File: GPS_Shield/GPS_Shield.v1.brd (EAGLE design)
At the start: 31.8 x 37.8 mm, 11 parts, among them T1 2N2222, U1 USD-SOCKETMOLEX-CORRECT

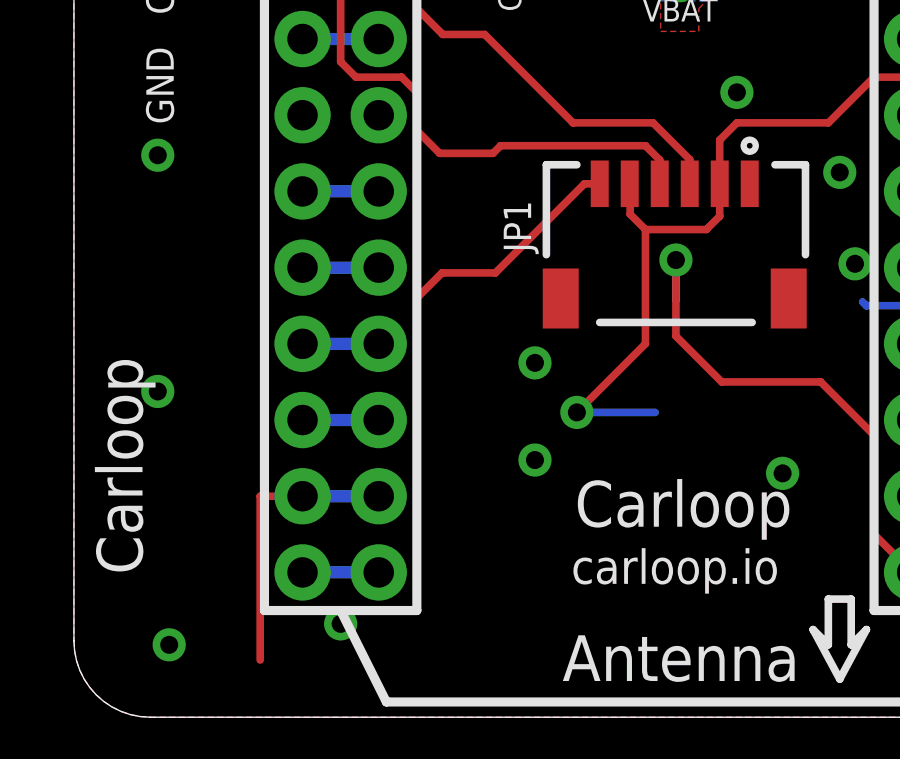
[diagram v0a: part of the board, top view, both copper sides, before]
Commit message: Add GPS_EN
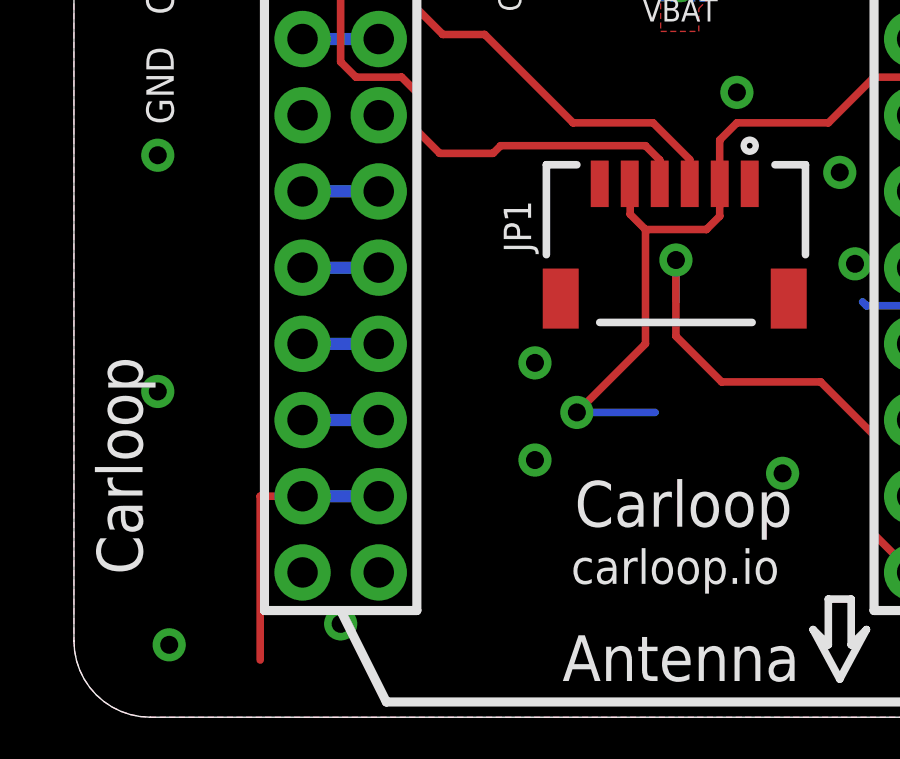
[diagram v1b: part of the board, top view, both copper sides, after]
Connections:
- removed net N$14: CORE.18, CORE.@18
- removed net N$15: CORE.17, CORE.@17
- new net GPS_EN: CORE.12, CORE.@12, GPS.19, JP1.6
- net PPS_EN: now also CORE.17, CORE.18, CORE.@17, CORE.@18; no longer CORE.12, CORE.@12, JP1.6
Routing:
- net PPS_EN: track 18.1 -> 5.08 mm
- net N$15: track 2.54 -> 0.00 mm
- net N$14: track 2.54 -> 0.00 mm
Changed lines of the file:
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@@
 <wire x1="31.242" y1="19.812" x2="28.702" y2="19.812" width="0.4064" layer="16"/>
-</signal>
-<signal name="N$14">
-<contactref element="CORE" pad="@18"/>
-<contactref element="CORE" pad="18"/>
-<wire x1="31.242" y1="17.272" x2="28.702" y2="17.272" width="0.4064" layer="16"/>
-</signal>
-<signal name="N$15">
-<contactref element="CORE" pad="@17"/>
-<contactref element="CORE" pad="17"/>
-<wire x1="31.242" y1="14.732" x2="28.702" y2="14.732" width="0.4064" layer="16"/>
 </signal>
 <signal name="N$26">
@@
 <signal name="PPS_EN">
 <contactref element="D1" pad="A"/>
-<contactref element="CORE" pad="12"/>
-<contactref element="CORE" pad="@12"/>
-<wire x1="10.922" y1="4.572" x2="8.382" y2="4.572" width="0.4064" layer="16"/>
-<contactref element="JP1" pad="6"/>
-<wire x1="18.288" y1="17.526" x2="17.78" y2="17.526" width="0.254" layer="1"/>
-<wire x1="14.8082" y1="14.5542" x2="13.0302" y2="14.5542" width="0.254" layer="1"/>
-<wire x1="13.0302" y1="14.5542" x2="12.192" y2="13.716" width="0.254" layer="1"/>
-<wire x1="12.192" y1="13.716" x2="12.192" y2="5.842" width="0.254" layer="1"/>
-<wire x1="14.8082" y1="14.5542" x2="17.78" y2="17.526" width="0.254" layer="1"/>
-<wire x1="8.382" y1="4.572" x2="-58.293" y2="-64.758" width="0" layer="19" extent="1-1"/>
-<wire x1="12.192" y1="5.842" x2="10.922" y2="4.572" width="0" layer="19" extent="1-1"/>
+<contactref element="CORE" pad="@18"/>
+<contactref element="CORE" pad="18"/>
+<wire x1="31.242" y1="17.272" x2="28.702" y2="17.272" width="0.4064" layer="16"/>
+<contactref element="CORE" pad="@17"/>
+<contactref element="CORE" pad="17"/>
+<wire x1="31.242" y1="14.732" x2="28.702" y2="14.732" width="0.4064" layer="16"/>
+<wire x1="28.702" y1="14.732" x2="-58.293" y2="-64.758" width="0" layer="19" extent="1-1"/>
+<wire x1="31.242" y1="17.272" x2="31.242" y2="14.732" width="0" layer="19" extent="1-1"/>
 </signal>
 <signal name="RST">
@@
 <wire x1="8.382" y1="19.812" x2="10.922" y2="19.812" width="0" layer="19" extent="1-1"/>
 </signal>
+<signal name="GPS_EN">
+<contactref element="CORE" pad="12"/>
+<contactref element="CORE" pad="@12"/>
+<contactref element="JP1" pad="6"/>
+<contactref element="GPS" pad="19"/>
+<wire x1="8.382" y1="4.572" x2="-9.017" y2="-58.039" width="0" layer="19" extent="1-1"/>
+<wire x1="10.922" y1="4.572" x2="8.382" y2="4.572" width="0" layer="19" extent="1-1"/>
+<wire x1="18.288" y1="17.526" x2="10.922" y2="4.572" width="0" layer="19" extent="1-1"/>
+</signal>
 </signals>

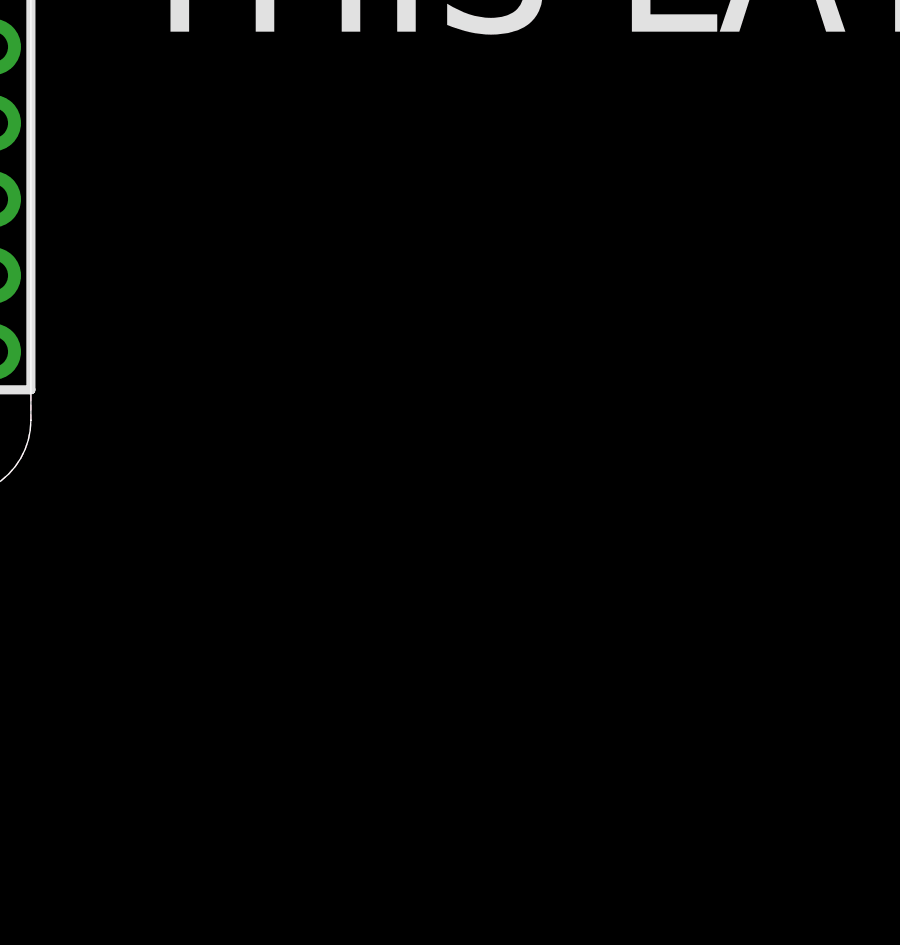
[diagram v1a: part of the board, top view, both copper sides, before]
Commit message: Tweaks for silkscreen
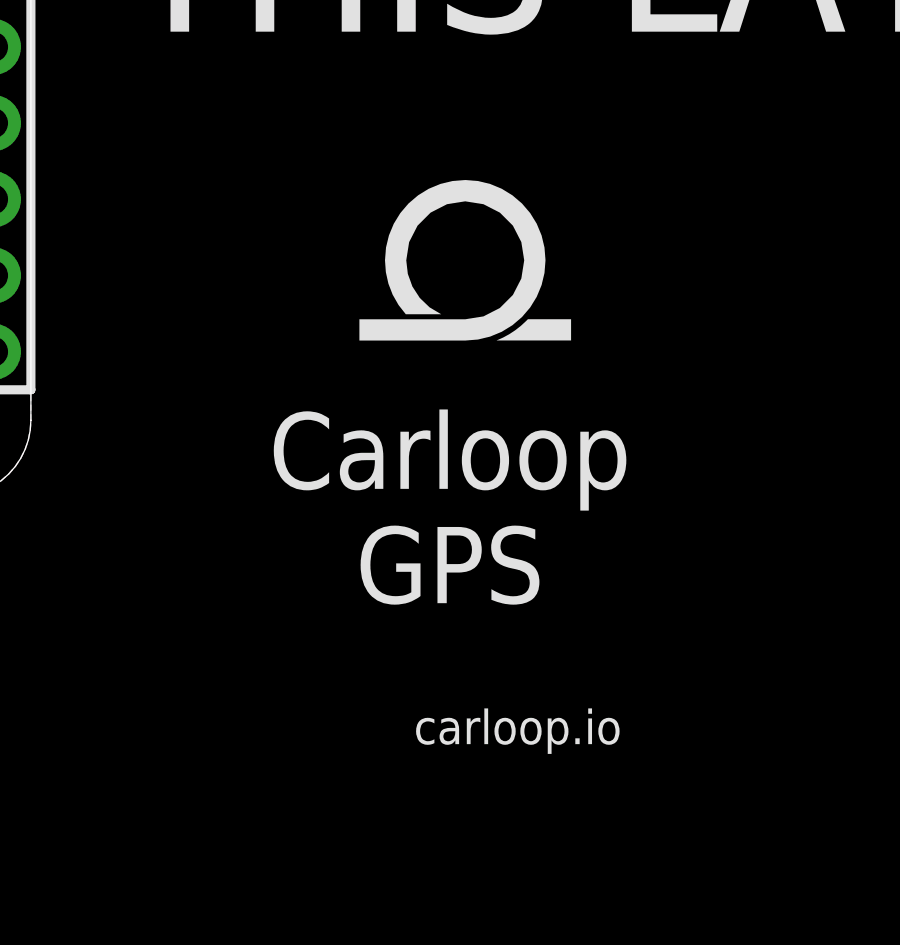
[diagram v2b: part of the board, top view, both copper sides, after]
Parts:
- added U$1: LOGO, MuniRent:CARLOOP
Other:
- board text added: "Carloop GPS"
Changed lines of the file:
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@@
 <grid distance="0.1" unitdist="inch" unit="inch" style="lines" multiple="1" display="yes" altdistance="0.025" altunitdist="inch" altunit="inch"/>
 <layers>
-<layer number="1" name="Top" color="4" fill="1" visible="yes" active="yes"/>
+<layer number="1" name="Top" color="4" fill="1" visible="no" active="yes"/>
 <layer number="2" name="Route2" color="1" fill="3" visible="no" active="no"/>
 <layer number="3" name="Route3" color="4" fill="3" visible="no" active="no"/>
 <layer number="14" name="Route14" color="1" fill="6" visible="no" active="no"/>
 <layer number="15" name="Route15" color="4" fill="6" visible="no" active="no"/>
-<layer number="16" name="Bottom" color="1" fill="1" visible="yes" active="yes"/>
-<layer number="17" name="Pads" color="2" fill="1" visible="yes" active="yes"/>
-<layer number="18" name="Vias" color="2" fill="1" visible="yes" active="yes"/>
-<layer number="19" name="Unrouted" color="6" fill="1" visible="yes" active="yes"/>
-<layer number="20" name="Dimension" color="15" fill="1" visible="yes" active="yes"/>
+<layer number="16" name="Bottom" color="1" fill="1" visible="no" active="yes"/>
+<layer number="17" name="Pads" color="2" fill="1" visible="no" active="yes"/>
+<layer number="18" name="Vias" color="2" fill="1" visible="no" active="yes"/>
+<layer number="19" name="Unrouted" color="6" fill="1" visible="no" active="yes"/>
+<layer number="20" name="Dimension" color="15" fill="1" visible="no" active="yes"/>
 <layer number="21" name="tPlace" color="7" fill="1" visible="yes" active="yes"/>
-<layer number="22" name="bPlace" color="7" fill="1" visible="yes" active="yes"/>
-<layer number="23" name="tOrigins" color="15" fill="1" visible="yes" active="yes"/>
-<layer number="24" name="bOrigins" color="15" fill="1" visible="yes" active="yes"/>
-<layer number="25" name="tNames" color="7" fill="1" visible="yes" active="yes"/>
-<layer number="26" name="bNames" color="7" fill="1" visible="yes" active="yes"/>
+<layer number="22" name="bPlace" color="7" fill="1" visible="no" active="yes"/>
+<layer number="23" name="tOrigins" color="15" fill="1" visible="no" active="yes"/>
+<layer number="24" name="bOrigins" color="15" fill="1" visible="no" active="yes"/>
+<layer number="25" name="tNames" color="7" fill="1" visible="no" active="yes"/>
+<layer number="26" name="bNames" color="7" fill="1" visible="no" active="yes"/>
 <layer number="27" name="tValues" color="7" fill="1" visible="no" active="yes"/>
 <layer number="28" name="bValues" color="7" fill="1" visible="no" active="yes"/>
-<layer number="29" name="tStop" color="7" fill="3" visible="yes" active="yes"/>
-<layer number="30" name="bStop" color="7" fill="6" visible="yes" active="yes"/>
-<layer number="31" name="tCream" color="7" fill="4" visible="yes" active="yes"/>
-<layer number="32" name="bCream" color="7" fill="5" visible="yes" active="yes"/>
+<layer number="29" name="tStop" color="7" fill="3" visible="no" active="yes"/>
+<layer number="30" name="bStop" color="7" fill="6" visible="no" active="yes"/>
+<layer number="31" name="tCream" color="7" fill="4" visible="no" active="yes"/>
+<layer number="32" name="bCream" color="7" fill="5" visible="no" active="yes"/>
 <layer number="33" name="tFinish" color="6" fill="3" visible="no" active="yes"/>
 <layer number="34" name="bFinish" color="6" fill="6" visible="no" active="yes"/>
@@
 <layer number="37" name="tTest" color="7" fill="1" visible="no" active="yes"/>
 <layer number="38" name="bTest" color="7" fill="1" visible="no" active="yes"/>
-<layer number="39" name="tKeepout" color="4" fill="11" visible="yes" active="yes"/>
-<layer number="40" name="bKeepout" color="1" fill="11" visible="yes" active="yes"/>
+<layer number="39" name="tKeepout" color="4" fill="11" visible="no" active="yes"/>
+<layer number="40" name="bKeepout" color="1" fill="11" visible="no" active="yes"/>
 <layer number="41" name="tRestrict" color="4" fill="10" visible="no" active="yes"/>
 <layer number="42" name="bRestrict" color="1" fill="10" visible="no" active="yes"/>
 <layer number="43" name="vRestrict" color="2" fill="10" visible="no" active="yes"/>
-<layer number="44" name="Drills" color="7" fill="1" visible="yes" active="yes"/>
-<layer number="45" name="Holes" color="7" fill="1" visible="yes" active="yes"/>
-<layer number="46" name="Milling" color="3" fill="1" visible="yes" active="yes"/>
+<layer number="44" name="Drills" color="7" fill="1" visible="no" active="yes"/>
+<layer number="45" name="Holes" color="7" fill="1" visible="no" active="yes"/>
+<layer number="46" name="Milling" color="3" fill="1" visible="no" active="yes"/>
 <layer number="47" name="Measures" color="7" fill="1" visible="no" active="yes"/>
 <layer number="48" name="Document" color="7" fill="1" visible="no" active="yes"/>
 <layer number="49" name="Reference" color="7" fill="1" visible="no" active="yes"/>
 <layer number="50" name="dxf" color="7" fill="1" visible="no" active="no"/>
-<layer number="51" name="tDocu" color="7" fill="1" visible="yes" active="yes"/>
+<layer number="51" name="tDocu" color="7" fill="1" visible="no" active="yes"/>
 <layer number="52" name="bDocu" color="7" fill="1" visible="no" active="yes"/>
 <layer number="53" name="tGND_GNDA" color="7" fill="9" visible="no" active="no"/>
@@
 <layer number="112" name="tSilk" color="7" fill="1" visible="no" active="yes"/>
 <layer number="113" name="IDFDebug" color="4" fill="1" visible="no" active="yes"/>
-<layer number="114" name="Badge_Outline" color="7" fill="1" visible="yes" active="yes"/>
-<layer number="115" name="ReferenceISLANDS" color="7" fill="1" visible="yes" active="yes"/>
+<layer number="114" name="Badge_Outline" color="7" fill="1" visible="no" active="yes"/>
+<layer number="115" name="ReferenceISLANDS" color="7" fill="1" visible="no" active="yes"/>
 <layer number="116" name="Patch_BOT" color="9" fill="4" visible="no" active="yes"/>
 <layer number="118" name="Rect_Pads" color="7" fill="1" visible="no" active="yes"/>
@@
 <layer number="230" name="230bmp" color="7" fill="1" visible="no" active="yes"/>
 <layer number="231" name="231bmp" color="7" fill="1" visible="no" active="yes"/>
-<layer number="232" name="Eagle3D_PG2" color="7" fill="1" visible="yes" active="yes"/>
-<layer number="233" name="Eagle3D_PG3" color="7" fill="1" visible="yes" active="yes"/>
+<layer number="232" name="Eagle3D_PG2" color="7" fill="1" visible="no" active="yes"/>
+<layer number="233" name="Eagle3D_PG3" color="7" fill="1" visible="no" active="yes"/>
 <layer number="248" name="Housing" color="7" fill="1" visible="no" active="yes"/>
 <layer number="249" name="Edge" color="7" fill="1" visible="no" active="yes"/>
@@
 <text x="35.56" y="15.24" size="5.08" layer="21">DO NOT USE
 THIS LAYOUT</text>
+<text x="46.482" y="2.54" size="2.54" layer="21" font="vector" ratio="16" rot="R180" align="bottom-center">Carloop
+GPS</text>
+<text x="48.7426" y="-7.366" size="1.143" layer="21" font="vector" ratio="16" rot="R180" align="bottom-center">carloop.io</text>
 </plain>
 <attributes>
@@
 <element name="C1" library="SparkFun-Passives" package="0603-CAP" value="1u" x="-68.58" y="-71.12"/>
 <element name="C2" library="SparkFun-Passives" package="0603-CAP" value="0.1u" x="-68.58" y="-73.66"/>
+<element name="U$1" library="MuniRent" package="CARLOOP" value="LOGO" x="43.18" y="5.08"/>
 </elements>
 <signals>
